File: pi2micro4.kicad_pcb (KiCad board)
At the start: 2 copper layers, 57.8 x 69.8 mm, 37 parts, among them K1 CONN_3, K2 CONN_3, K3 CONN_S7, K4 CONN_S10, K5 CONN_S8, K6 CONN_S11, K7 CONN_S9, K8 CONN_S12, M1 microduino_base, M2 microduino_base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

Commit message: mejorando planos de tierra
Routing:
- net GND: track 270.8 -> 362.0 mm, vias 1 -> 22

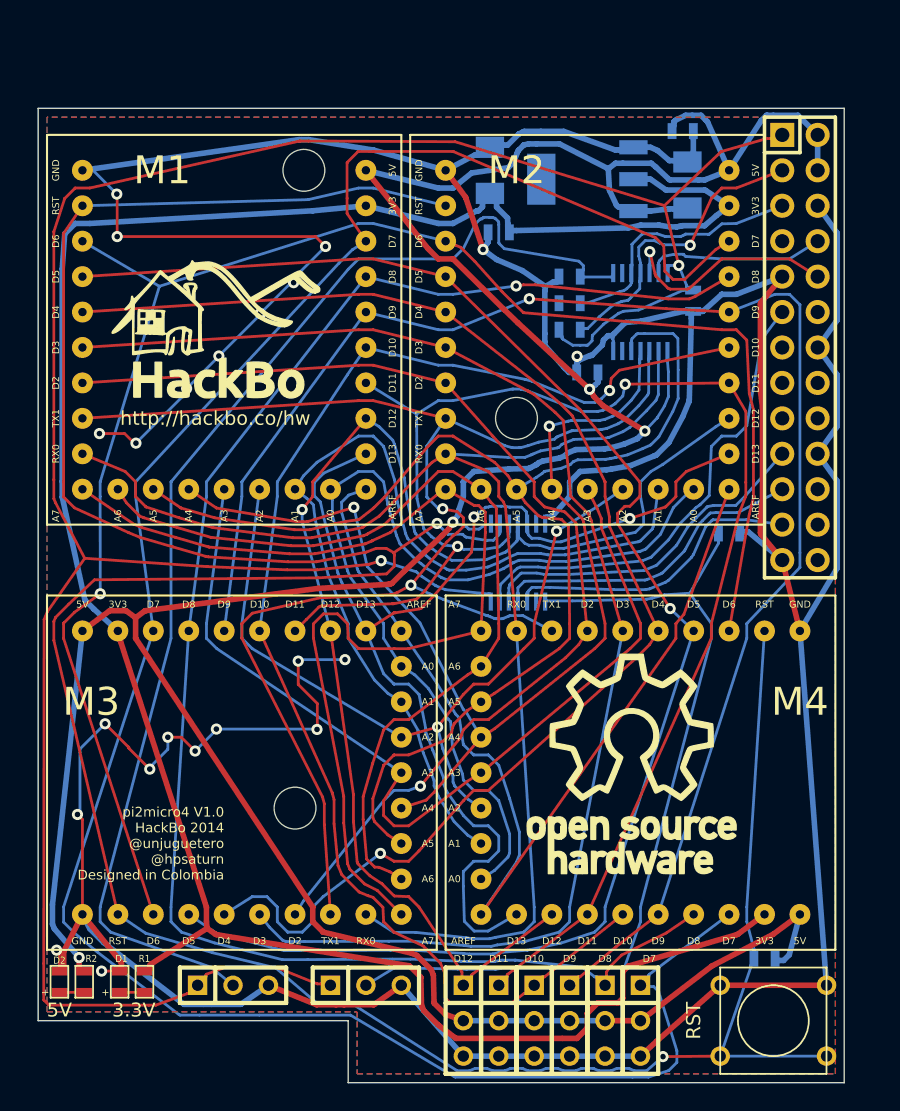
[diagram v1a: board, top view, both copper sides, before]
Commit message: conectores de entrada analoga y uart a las raspberry pi
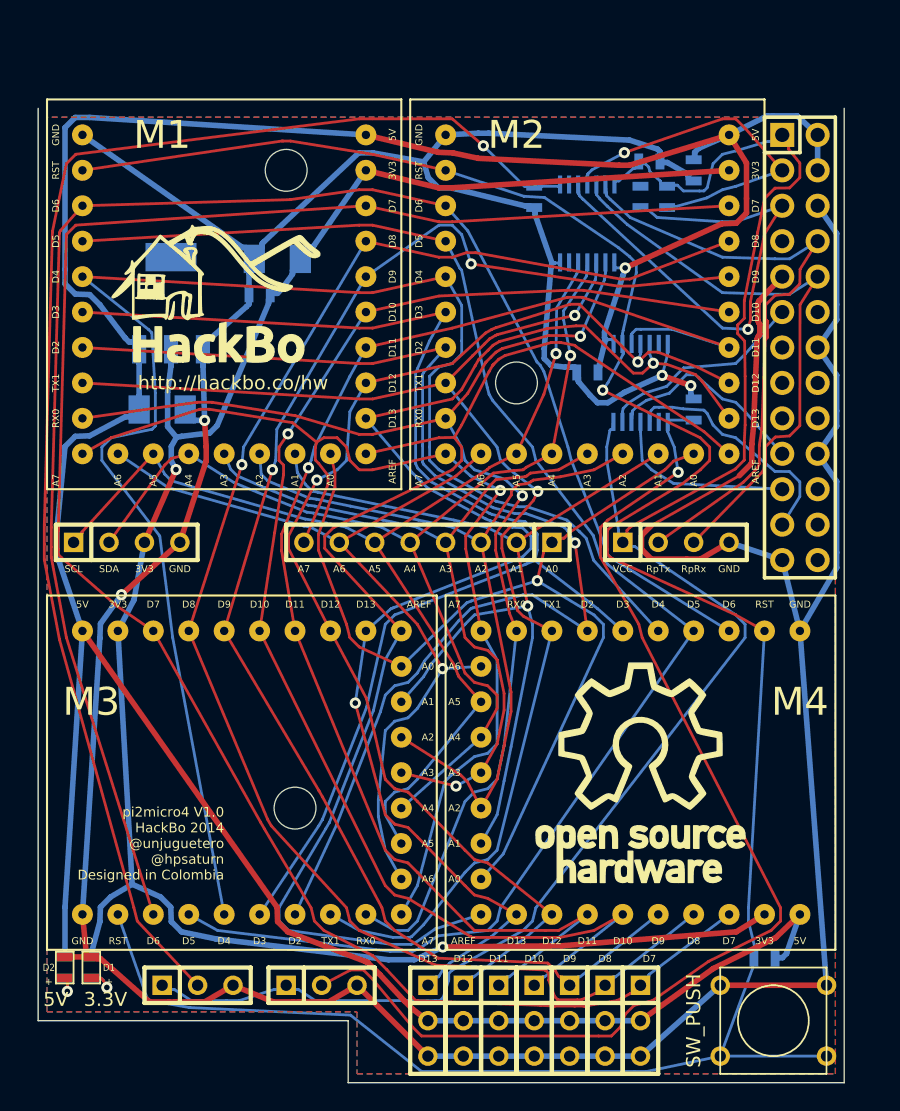
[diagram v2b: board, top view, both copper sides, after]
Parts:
- added K9: CONN_S12, SIL-3, F.Cu at (128.3, 147.3)
- added P2: CONN_I2C, SIL-4, F.Cu at (106.7, 113.0)
- added P3: CONN_PI_TXRX, SIL-4, F.Cu at (146.1, 113.0)
- added P4: CONN_01X08, Connect:SIL-8, F.Cu at (128.3, 113.0)
- MH1, MH2, MH3: value MountingHole_3mm_RevA_Date21Jun2010 -> MountingHole_4mm_RevA_Date21Jun2010
- R1, R2: moved to B.Cu
- SW1: value RST -> SW_PUSH
- moved C3 41.0 mm to (109.2, 103.5), turned to 0 degrees
- moved U1 31.1 mm to (109.9, 95.9), turned to 180 degrees
- moved C2 17.7 mm to (116.2, 95.2)
- moved C1 16.5 mm to (117.5, 92.7), turned to 180 degrees
- moved U3 15.6 mm to (143.5, 101.6)
- moved R5 11.8 mm to (145.4, 88.3), turned to 270 degrees
- moved C6 10.5 mm to (144.1, 85.7), turned to 0 degrees
- moved R3 9.25 mm to (147.3, 103.5), turned to 90 degrees
- moved R6 9.16 mm to (143.5, 88.3), turned to 270 degrees
- moved U2 7.41 mm to (139.7, 90.2)
- moved R4 6.25 mm to (135.9, 88.3), turned to 270 degrees
- moved R1 3.94 mm to (104.1, 143.5)
- moved K1 3.17 mm to (120.7, 144.8)
- moved C4 2.92 mm to (147.3, 86.4), turned to 270 degrees
- moved G1 2.54 mm to (113.0, 96.5)
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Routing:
- net /3V3_RB: track 185.1 -> 128.6 mm, vias 2 -> 0
- net GND: track 362.0 -> 306.8 mm, vias 22 -> 4
- net /RST: track 216.0 -> 172.1 mm, vias 2 -> 1
- net /Rp_TX: track 12.8 -> 44.7 mm
- net /Rp_RX: track 16.5 -> 42.4 mm, vias 1 -> 0
- net /D7: track 157.6 -> 137.6 mm
- net /AREF: track 72.4 -> 92.3 mm
- net +3.3V: track 164.9 -> 145.1 mm, vias 0 -> 2
- net /Rp_RST: track 34.1 -> 15.1 mm
- net /Rp_SCL: track 18.5 -> 36.6 mm, vias 0 -> 1
- net /D4: track 97.6 -> 115.0 mm, vias 1 -> 0
- net Net-(K1-Pad2): track 66.7 -> 82.1 mm, vias 0 -> 1
- net /D13: track 81.8 -> 96.2 mm
- net Net-(K2-Pad2): track 87.0 -> 99.4 mm, vias 0 -> 1
- net /TX1: track 106.9 -> 95.3 mm
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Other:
- board text added: "3V3"
- board text added: "A0"
- board text added: "A1"
- board text added: "A2"
- board text added: "A3"
- board text added: "A4"
- board text added: "A5"
- board text added: "A6"
- board text added: "A7"
- board text added: "D13"
- board text added: "GND"
- board text added: "RpRx"
- board text added: "RpTx"
- board text added: "SCL"
- board text added: "SDA"
- board text added: "VCC"

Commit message: D13 led
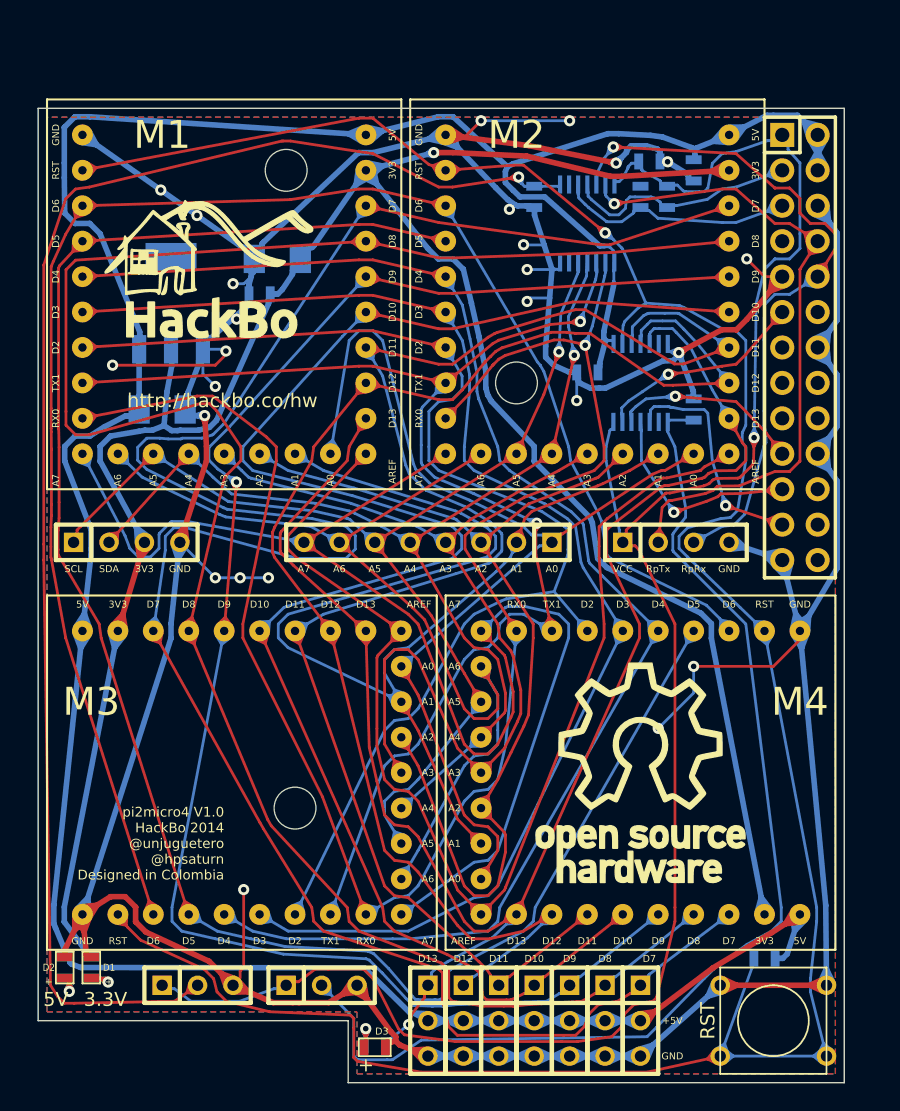
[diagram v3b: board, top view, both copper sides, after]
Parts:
- added D3: LED, SMD-0603, F.Cu at (124.5, 149.2)
- added R8: R, SMD-0603, B.Cu at (124.5, 149.1)
- SW1: value SW_PUSH -> RST
- moved G1 1.85 mm to (112.5, 94.7)
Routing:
- net GND: track 306.8 -> 457.6 mm, vias 4 -> 25
- net /RX0: track 90.3 -> 133.4 mm, vias 2 -> 1
- net +3.3V: track 145.1 -> 187.3 mm, vias 2 -> 1
- net /D8: track 111.1 -> 151.0 mm, vias 1 -> 0
- net +5V: track 225.0 -> 262.9 mm, vias 1 -> 0
- net /A7: track 75.6 -> 110.1 mm, vias 1 -> 0
- net /D13: track 96.2 -> 128.7 mm, vias 2 -> 1
- net /A1: track 64.5 -> 96.3 mm, vias 1 -> 0
- net /D5: track 108.8 -> 139.0 mm
- net /D10: track 98.2 -> 127.7 mm, vias 1 -> 0
- net /RST: track 172.1 -> 198.4 mm
- net /A3: track 54.8 -> 81.0 mm, vias 1 -> 0
- net /D7: track 137.6 -> 162.9 mm
- net /D12: track 86.8 -> 111.6 mm, vias 2 -> 0
- net /D9: track 103.6 -> 128.4 mm, vias 2 -> 1
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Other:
- board text added: "+5V"

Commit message: mounting holes replacement
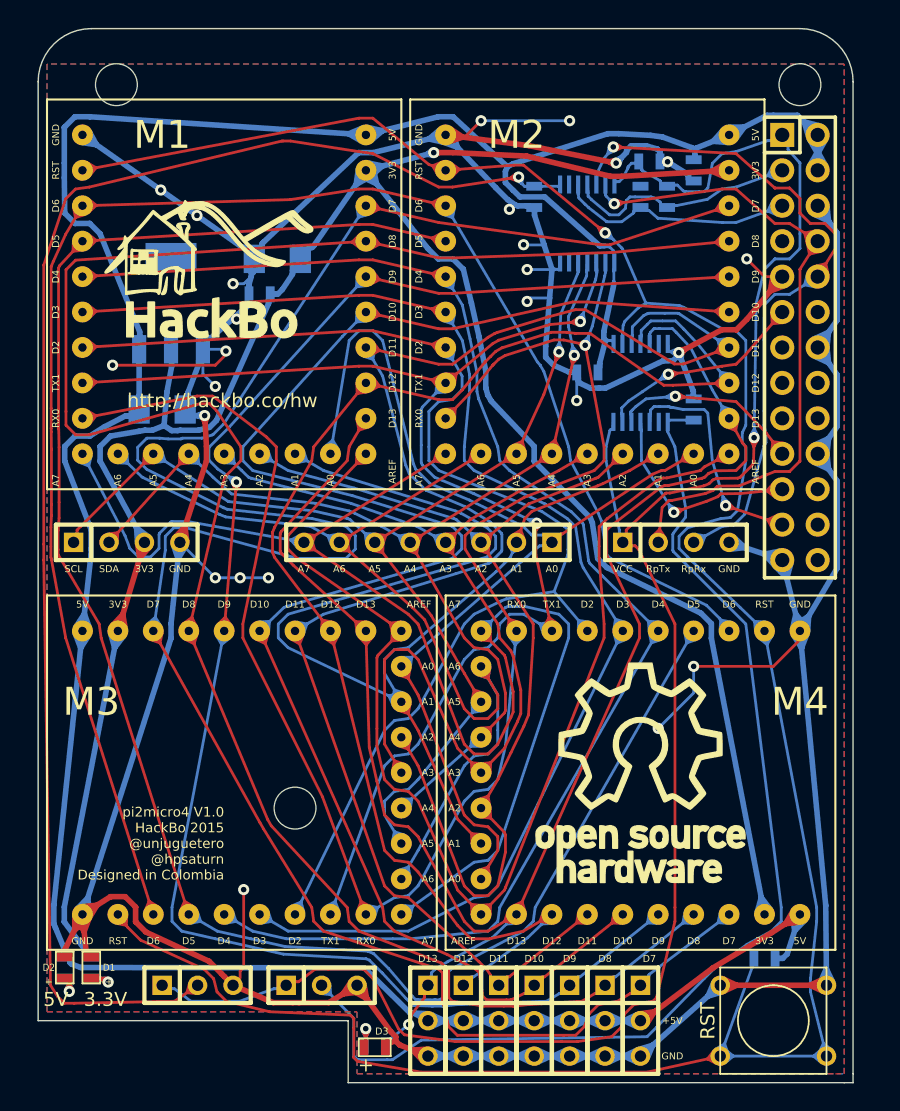
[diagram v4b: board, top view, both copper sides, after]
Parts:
- moved MH1 37.3 mm to (154.9, 80.2)
- moved MH2 35.8 mm to (105.9, 80.2)
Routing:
- net GND: track 457.6 -> 446.9 mm, vias 25 -> 24
- net (no net): track 0.00 -> 6.46 mm, vias 0 -> 1
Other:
- board size 57.8 x 69.8 mm -> 58.4 x 75.6 mm
- board text added: "pi2micro4 V1.0 HackBo 2015 @unjuguetero @hpsaturn Designed in Colombia"
- board text removed: "pi2micro4 V1.0 HackBo 2014 @unjuguetero @hpsaturn Designed in Colombia"
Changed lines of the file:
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@@
-(kicad_pcb (version 4) (host pcbnew "(2014-08-05 BZR 5054)-product")
+(kicad_pcb (version 4) (host pcbnew "(2015-04-08 BZR 5585)-product")
   (general
     (links 190)
@@
     (area 95.100073 75.89 169.925 158.910001)
     (thickness 1.6)
-    (drawings 41)
-    (tracks 2335)
+    (drawings 44)
+    (tracks 2332)
     (zones 0)
     (modules 43)
@@
   )
   (module Mounting_Holes:MountingHole_3mm (layer F.Cu)
-    (at 118.11 86.36)
+    (at 154.94 80.22)
     (descr "Mounting hole, Befestigungsbohrung, 3mm, No Annular, Kein Restring,")
     (tags "Mounting hole, Befestigungsbohrung, 3mm, No Annular, Kein Restring,")
@@
   )
   (module Mounting_Holes:MountingHole_3mm (layer F.Cu)
-    (at 134.62 101.6)
+    (at 105.94 80.22)
     (descr "Mounting hole, Befestigungsbohrung, 3mm, No Annular, Kein Restring,")
     (tags "Mounting hole, Befestigungsbohrung, 3mm, No Annular, Kein Restring,")
@@
     (pad 1 thru_hole circle (at 0 0) (size 2.99974 2.99974) (drill 2.99974) (layers))
   )
-  (gr_line (start 158.115 81.915) (end 100.33 81.915) (angle 90) (layer Edge.Cuts) (width 0.1))
+  (gr_line (start 158.75 151.765) (end 158.115 151.765) (angle 90) (layer Edge.Cuts) (width 0.1))
+  (gr_line (start 158.75 151.13) (end 158.75 151.765) (angle 90) (layer Edge.Cuts) (width 0.1))
+  (gr_line (start 158.75 80.01) (end 158.75 151.13) (angle 90) (layer Edge.Cuts) (width 0.1))
+  (gr_line (start 100.33 80.01) (end 100.33 147.32) (angle 90) (layer Edge.Cuts) (width 0.1))
+  (gr_line (start 154.94 76.2) (end 104.14 76.2) (angle 90) (layer Edge.Cuts) (width 0.1))
+  (gr_arc (start 154.94 80.01) (end 154.94 76.2) (angle 90) (layer Edge.Cuts) (width 0.1))
+  (gr_arc (start 104.14 80.01) (end 100.33 80.01) (angle 90) (layer Edge.Cuts) (width 0.1))
   (gr_text GND (at 145.796 149.86) (layer F.SilkS)
     (effects (font (size 0.5 0.5) (thickness 0.125)))
@@
     (effects (font (size 0.5 0.5) (thickness 0.125)))
   )
-  (gr_line (start 158.115 151.765) (end 158.115 81.915) (angle 90) (layer Edge.Cuts) (width 0.1))
   (gr_line (start 122.555 151.765) (end 158.115 151.765) (angle 90) (layer Edge.Cuts) (width 0.1))
   (gr_line (start 122.555 147.32) (end 122.555 151.765) (angle 90) (layer Edge.Cuts) (width 0.1))
   (gr_line (start 100.33 147.32) (end 122.555 147.32) (angle 90) (layer Edge.Cuts) (width 0.1))
-  (gr_line (start 100.33 81.915) (end 100.33 147.32) (angle 90) (layer Edge.Cuts) (width 0.1))
   (dimension 69.85 (width 0.3) (layer Cmts.User)
     (gr_text "69,850 mm" (at 163.275 116.84 270) (layer Cmts.User)
@@
     (arrow2b (pts (xy 161.925 81.915) (xy 162.511421 83.041504)))
   )
-  (dimension 57.785 (width 0.3) (layer Cmts.User)
-    (gr_text "57,785 mm" (at 129.2225 77.39) (layer Cmts.User)
-      (effects (font (size 1.5 1.5) (thickness 0.3)))
-    )
-    (feature1 (pts (xy 158.115 80.645) (xy 158.115 76.04)))
-    (feature2 (pts (xy 100.33 80.645) (xy 100.33 76.04)))
-    (crossbar (pts (xy 100.33 78.74) (xy 158.115 78.74)))
-    (arrow1a (pts (xy 158.115 78.74) (xy 156.988496 79.326421)))
-    (arrow1b (pts (xy 158.115 78.74) (xy 156.988496 78.153579)))
-    (arrow2a (pts (xy 100.33 78.74) (xy 101.456504 79.326421)))
-    (arrow2b (pts (xy 100.33 78.74) (xy 101.456504 78.153579)))
-  )
   (dimension 34.925 (width 0.3) (layer Cmts.User)
     (gr_text "34,925 mm" (at 140.6525 157.56) (layer Cmts.User)
@@
     (effects (font (size 1 1) (thickness 0.25)))
   )
-  (gr_text "pi2micro4 V1.0\nHackBo 2014\n@unjuguetero\n@hpsaturn\nDesigned in Colombia\n" (at 113.665 134.62) (layer F.SilkS)
+  (gr_text "pi2micro4 V1.0\nHackBo 2015\n@unjuguetero\n@hpsaturn\nDesigned in Colombia\n" (at 113.665 134.62) (layer F.SilkS)
     (effects (font (size 0.7 0.7) (thickness 0.125)) (justify right))
   )
@@
     (effects (font (size 0.508 0.508) (thickness 0.127)))
   )
+  (segment (start 114.808 144.272) (end 114.808 143.764) (width 0.2) (layer F.Cu) (net 0))
+  (via (at 115.062 137.922) (size 0.8) (layers F.Cu B.Cu) (net 0))
+  (segment (start 115.062 143.51) (end 115.062 137.922) (width 0.2) (layer F.Cu) (net 0))
+  (segment (start 114.808 143.764) (end 115.062 143.51) (width 0.2) (layer F.Cu) (net 0))
   (segment (start 141.3256 91.8786) (end 140.8836 91.7749) (width 0.2) (layer B.Cu) (net 1))
   (segment (start 141.5805 92.1335) (end 141.3256 91.8786) (width 0.2) (layer B.Cu) (net 1))
@@
   (segment (start 130.5271 86.2849) (end 130.0027 86.8164) (width 0.2) (layer F.Cu) (net 26))
   (segment (start 130.5271 86.2849) (end 129.9283 85.8388) (width 0.2) (layer F.Cu) (net 26))
-  (segment (start 153.67 93.98) (end 152.4 93.98) (width 0.2) (layer F.Cu) (net 27) (status 400000))
+  (segment (start 153.67 93.98) (end 152.4 93.98) (width 0.2) (layer F.Cu) (net 27))
   (via (at 151.13 92.71) (size 0.8) (layers F.Cu B.Cu) (net 27))
   (segment (start 152.4 93.98) (end 151.13 92.71) (width 0.2) (layer F.Cu) (net 27))
@@
   (segment (start 113.03 100.33) (end 105.664 100.33) (width 0.2) (layer F.Cu) (net 27))
   (segment (start 113.792 99.568) (end 113.03 100.33) (width 0.2) (layer F.Cu) (net 27))
-  (segment (start 114.808 144.272) (end 114.808 143.764) (width 0.2) (layer F.Cu) (net 27))
-  (via (at 115.062 137.922) (size 0.8) (layers F.Cu B.Cu) (net 27))
-  (segment (start 115.062 143.51) (end 115.062 137.922) (width 0.2) (layer F.Cu) (net 27))
-  (segment (start 114.808 143.764) (end 115.062 143.51) (width 0.2) (layer F.Cu) (net 27))
   (segment (start 136.601753 91.710222) (end 135.144222 91.710222) (width 0.2) (layer B.Cu) (net 27))
   (via (at 135.128 91.694) (size 0.8) (layers F.Cu B.Cu) (net 27))
@@
   (segment (start 117.1837 146.0285) (end 118.5807 146.0285) (width 0.4) (layer F.Cu) (net 27))
   (segment (start 114.3 144.78) (end 117.1837 146.0285) (width 0.4) (layer F.Cu) (net 27))
-  (segment (start 113.4765 143.9531) (end 114.3 144.78) (width 0.4) (layer F.Cu) (net 27))
+  (segment (start 113.4765 143.9531) (end 113.666311 144.143695) (width 0.4) (layer F.Cu) (net 27))
+  (segment (start 113.666311 144.143695) (end 114.3 144.78) (width 0.4) (layer F.Cu) (net 27))
   (segment (start 112.5869 143.0635) (end 113.4765 143.9531) (width 0.4) (layer F.Cu) (net 27))
   (segment (start 108.0574 140.9685) (end 112.5869 143.0635) (width 0.4) (layer F.Cu) (net 27))
@@
   (segment (start 122.1871 145.399) (end 122.7733 144.5064) (width 0.4) (layer F.Cu) (net 27))
   (segment (start 122.1871 145.399) (end 123.2479 145.2752) (width 0.4) (layer F.Cu) (net 27))
-  (segment (start 115.3815 145.2482) (end 114.314 145.2783) (width 0.4) (layer F.Cu) (net 27))
-  (segment (start 115.3815 145.2482) (end 114.673 144.4493) (width 0.4) (layer F.Cu) (net 27))
-  (segment (start 113.4765 143.9531) (end 114.4691 144.311) (width 0.4) (layer F.Cu) (net 27))
-  (segment (start 113.4765 143.9531) (end 113.8303 144.9472) (width 0.4) (layer F.Cu) (net 27))
   (segment (start 104.5455 139.0441) (end 103.9753 139.9851) (width 0.4) (layer F.Cu) (net 27))
   (segment (start 104.5455 139.0441) (end 103.4507 139.1527) (width 0.4) (layer F.Cu) (net 27))
@@
     (polygon
       (pts
-        (xy 100.965 146.685) (xy 123.19 146.685) (xy 123.19 151.13) (xy 157.48 151.13) (xy 157.48 82.55)
-        (xy 100.965 82.55) (xy 100.965 85.725)
+        (xy 100.965 146.685) (xy 123.19 146.685) (xy 123.19 151.13) (xy 158.115 151.13) (xy 158.115 78.74)
+        (xy 100.965 78.74) (xy 100.965 85.725)
       )
     )
@@
     (polygon
       (pts
-        (xy 100.965 146.685) (xy 123.19 146.685) (xy 123.19 151.13) (xy 157.48 151.13) (xy 157.48 82.55)
-        (xy 100.965 82.55) (xy 100.965 85.725)
+        (xy 100.965 146.685) (xy 123.19 146.685) (xy 123.19 151.13) (xy 157.48 151.13) (xy 158.115 151.13)
+        (xy 158.115 78.74) (xy 100.965 78.74) (xy 100.965 85.725)
       )
     )
